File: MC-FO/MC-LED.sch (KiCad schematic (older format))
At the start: 14 parts, among them U21 TPS3703A5330DSER, U22 74ACT08SCX, U23 TPS3703A5500DSER, U24 TPS3703A5330DSER

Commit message: floating pins fix, signal name updates
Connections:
- wire segments 70 -> 76
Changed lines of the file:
@@
 	2550 2150 2500 2150
 Wire Wire Line
-	2500 2150 2500 2750
+	2500 2150 2500 2550
 Wire Wire Line
 	2500 2750 2400 2750
@@
 	4800 2150 4750 2150
 Wire Wire Line
-	4750 2150 4750 2750
+	4750 2150 4750 2550
 Wire Wire Line
 	4750 2750 4650 2750
@@
 	9350 2150 9250 2150
 Wire Wire Line
-	9250 2150 9250 2750
+	9250 2150 9250 2550
 Wire Wire Line
 	9250 2750 9000 2750
@@
 U 1 1 61797676
 P 3750 5000
+AR Path="/61797676" Ref="D1"  Part="1"
+AR Path="/6175812E/61797676" Ref="D1"  Part="1"
 F 0 "D1" V 3789 4782 50  0000 R CNN
 F 1 "550-2207-004F" V 3698 4782 50  0000 R CNN
@@
 U 1 1 6179851C
 P 9300 4000
+AR Path="/6179851C" Ref="D2"  Part="1"
+AR Path="/6175812E/6179851C" Ref="D2"  Part="1"
 F 0 "D2" V 9339 3782 50  0000 R CNN
 F 1 "550-2207-004F" V 9248 3782 50  0000 R CNN
@@
 	0    -1   -1   0
 $EndComp
+Wire Wire Line
+	9250 2550 9000 2550
+Connection ~ 9250 2550
+Wire Wire Line
+	9250 2550 9250 2750
+Wire Wire Line
+	4750 2550 4650 2550
+Connection ~ 4750 2550
+Wire Wire Line
+	4750 2550 4750 2750
+Wire Wire Line
+	2400 2550 2500 2550
+Connection ~ 2500 2550
+Wire Wire Line
+	2500 2550 2500 2750
 $EndSCHEMATC

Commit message: Fixed floating pins, added notes
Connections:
- wire segments 76 -> 100
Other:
- note added: "Voltage Drop Considerations?\n"
- moved on the sheet: R20
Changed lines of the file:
@@
 Comment4 ""
 $EndDescr
-Text Notes 2750 6050 0    50   ~ 10
+Text Notes 2750 6350 0    50   ~ 10
 Power Indicator LED CKT
 $Comp
 L Device:R_US R20
 U 1 1 61706570
-P 3850 4350
-F 0 "R20" H 3700 4250 50  0000 C CNN
-F 1 "500 Ohm" H 3600 4350 50  0000 C CNN
-F 2 "Resistor_SMD:R_0603_1608Metric" V 3890 4340 50  0001 C CNN
-F 3 "~" H 3850 4350 50  0001 C CNN
-	1    3850 4350
+P 3850 4650
+F 0 "R20" H 3700 4550 50  0000 C CNN
+F 1 "500 Ohm" H 3600 4650 50  0000 C CNN
+F 2 "Resistor_SMD:R_0603_1608Metric" V 3890 4640 50  0001 C CNN
+F 3 "~" H 3850 4650 50  0001 C CNN
+	1    3850 4650
 	-1   0    0    1
 $EndComp
 Wire Wire Line
-	3850 5150 3850 5450
+	3850 5450 3850 5750
 Text Notes 8350 4950 0    50   ~ 10
 Module Status LED CKT
@@
 	9400 4150 9400 4450
 Wire Wire Line
-	3850 5450 4050 5450
+	3850 5750 4050 5750
 Text HLabel 7950 2150 0    50   Input ~ 0
 StatusLED
-Text HLabel 4050 5450 2    50   Input ~ 0
+Text HLabel 4050 5750 2    50   Input ~ 0
 GND1
 Text HLabel 9650 4450 2    50   Input ~ 0
@@
 	4900 2950 4900 3900
 Wire Wire Line
-	3400 4000 3850 4000
-Wire Wire Line
-	3850 4000 3850 4200
-Wire Wire Line
-	3850 4500 3850 4850
+	3850 4300 3850 4500
+Wire Wire Line
+	3850 4800 3850 5150
 Text HLabel 2950 2150 2    50   Input ~ 0
 3V3
@@
 L Existing_IC_Models:550-0207-010-1163401 D1
 U 1 1 61797676
-P 3750 5000
+P 3750 5300
 AR Path="/61797676" Ref="D1"  Part="1"
 AR Path="/6175812E/61797676" Ref="D1"  Part="1"
-F 0 "D1" V 3789 4782 50  0000 R CNN
-F 1 "550-2207-004F" V 3698 4782 50  0000 R CNN
-F 2 "Footprints_MC-FO:550-2207-004F" H 3750 5100 50  0001 C CNN
-F 3 "" H 3750 5100 50  0001 C CNN
-	1    3750 5000
+F 0 "D1" V 3789 5082 50  0000 R CNN
+F 1 "550-2207-004F" V 3698 5082 50  0000 R CNN
+F 2 "Footprints_MC-FO:550-2207-004F" H 3750 5400 50  0001 C CNN
+F 3 "" H 3750 5400 50  0001 C CNN
+	1    3750 5300
 	0    -1   -1   0
 $EndComp
@@
 Wire Wire Line
 	2500 2550 2500 2750
+Text Notes 8200 1700 0    50   ~ 0
+Voltage Drop Considerations?\n
+Wire Wire Line
+	2600 3900 2400 3900
+Wire Wire Line
+	2400 3900 2400 4200
+Wire Wire Line
+	2400 4200 2600 4200
+Wire Wire Line
+	2400 4200 2400 4550
+Wire Wire Line
+	2400 4550 3500 4550
+Wire Wire Line
+	3500 4550 3500 4300
+Wire Wire Line
+	3500 4300 3400 4300
+Connection ~ 2400 4200
+Wire Wire Line
+	3500 4300 3850 4300
+Connection ~ 3500 4300
+Wire Wire Line
+	3650 4000 3650 4100
+Wire Wire Line
+	3400 4000 3650 4000
+Wire Wire Line
+	3400 4100 3650 4100
+Wire Wire Line
+	3650 4100 3650 4700
+Wire Wire Line
+	3650 4700 2300 4700
+Wire Wire Line
+	2300 4700 2300 4100
+Wire Wire Line
+	2300 3800 2600 3800
+Connection ~ 3650 4100
+Wire Wire Line
+	2300 4100 2600 4100
+Connection ~ 2300 4100
+Wire Wire Line
+	2300 4100 2300 3800
+Text HLabel 2050 3450 0    50   Input ~ 0
+5V
+Text HLabel 4050 3700 2    50   Input ~ 0
+5V
+Wire Wire Line
+	4050 3700 3800 3700
+Wire Wire Line
+	3800 3700 3800 4200
+Wire Wire Line
+	3800 4200 3400 4200
+Wire Wire Line
+	2050 3450 2150 3450
+Wire Wire Line
+	2150 3450 2150 3700
+Wire Wire Line
+	2150 3700 2600 3700
+Wire Wire Line
+	2150 3700 2150 4000
+Wire Wire Line
+	2150 4000 2600 4000
+Connection ~ 2150 3700
 $EndSCHEMATC

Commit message: unpopulated cap after voltage regulators
and changed reference designator numbering scheme
and moved the or gate that sends 3.3 V to comparator in detector ckt
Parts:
- D181: renamed from D1; symbol Existing_IC_Models:550-0207-010-1163401 -> Existing_IC_Models:550-2207-004F
- D182: renamed from D2; symbol Existing_IC_Models:550-0207-010-1163401 -> Existing_IC_Models:550-2207-004F
- renumbered C35 to C181, C36 to C182, C37 to C183, R19 to R181, R20 to R182, R21 to R183, R22 to R184, R23 to R185, U21 to U181, U22 to U182, U23 to U183, U24 to U184
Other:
- note added: "add comparatorson both and logically AND together for LED on power status\n\n\n (windowed comparators or voltage supervisors)"
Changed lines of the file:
@@
 Power Indicator LED CKT
 $Comp
-L Device:R_US R20
+L Device:R_US R182
 U 1 1 61706570
 P 3850 4650
-F 0 "R20" H 3700 4550 50  0000 C CNN
+F 0 "R182" H 3700 4550 50  0000 C CNN
 F 1 "500 Ohm" H 3600 4650 50  0000 C CNN
 F 2 "Resistor_SMD:R_0603_1608Metric" V 3890 4640 50  0001 C CNN
@@
 Module Status LED CKT
 $Comp
-L Device:R_US R22
+L Device:R_US R184
 U 1 1 61713526
 P 9400 3450
-F 0 "R22" H 9250 3350 50  0000 C CNN
+F 0 "R184" H 9250 3350 50  0000 C CNN
 F 1 "500 Ohm" H 9150 3450 50  0000 C CNN
 F 2 "Resistor_SMD:R_0603_1608Metric" V 9440 3440 50  0001 C CNN
@@
 5V
 $Comp
-L Existing_IC_Models:74ACT08SCX U22
+L Existing_IC_Models:74ACT08SCX U182
 U 1 1 6176E3CF
 P 3000 3550
-F 0 "U22" H 3000 3665 50  0000 C CNN
+F 0 "U182" H 3000 3665 50  0000 C CNN
 F 1 "74ACT08SCX" H 3000 3574 50  0000 C CNN
 F 2 "Package_SO:SOIC-14_3.9x8.7mm_P1.27mm" H 3000 3550 50  0001 C CNN
@@
 $EndComp
 $Comp
-L Existing_IC_Models:TPS3703A5500DSER U23
+L Existing_IC_Models:TPS3703A5500DSER U183
 U 1 1 6177F576
 P 4250 2250
-F 0 "U23" H 4250 2215 50  0000 C CNN
+F 0 "U183" H 4250 2215 50  0000 C CNN
 F 1 "TPS3703A5500DSER" H 4250 2124 50  0000 C CNN
 F 2 "Package_SON:WSON-6_1.5x1.5mm_P0.5mm" H 4250 2250 50  0001 C CNN
@@
 $EndComp
 $Comp
-L Existing_IC_Models:TPS3703A5330DSER U21
+L Existing_IC_Models:TPS3703A5330DSER U181
 U 1 1 61781150
 P 2000 2250
-F 0 "U21" H 2000 2215 50  0000 C CNN
+F 0 "U181" H 2000 2215 50  0000 C CNN
 F 1 "TPS3703A5330DSER" H 2000 2124 50  0000 C CNN
 F 2 "Package_SON:WSON-6_1.5x1.5mm_P0.5mm" H 2000 2250 50  0001 C CNN
@@
 3V3
 $Comp
-L Device:R_Small_US R19
+L Device:R_Small_US R181
 U 1 1 617C2D42
 P 2900 2700
-F 0 "R19" H 2968 2746 50  0000 L CNN
+F 0 "R181" H 2968 2746 50  0000 L CNN
 F 1 "10 K" H 2968 2655 50  0000 L CNN
 F 2 "Resistor_SMD:R_0603_1608Metric" H 2900 2700 50  0001 C CNN
@@
 $EndComp
 $Comp
-L Device:R_Small_US R21
+L Device:R_Small_US R183
 U 1 1 617C3F20
 P 5200 2550
-F 0 "R21" H 5268 2596 50  0000 L CNN
+F 0 "R183" H 5268 2596 50  0000 L CNN
 F 1 "10 K" H 5268 2505 50  0000 L CNN
 F 2 "Resistor_SMD:R_0603_1608Metric" H 5200 2550 50  0001 C CNN
@@
 Connection ~ 4900 2950
 $Comp
-L Device:C_Small C35
+L Device:C_Small C181
 U 1 1 617CFF8B
 P 1350 3100
-F 0 "C35" H 1442 3146 50  0000 L CNN
+F 0 "C181" H 1442 3146 50  0000 L CNN
 F 1 "1 uF" H 1442 3055 50  0000 L CNN
 F 2 "Capacitor_SMD:C_0603_1608Metric" H 1350 3100 50  0001 C CNN
@@
 $EndComp
 $Comp
-L Device:C_Small C36
+L Device:C_Small C182
 U 1 1 617D05D8
 P 3800 3300
-F 0 "C36" H 3892 3346 50  0000 L CNN
+F 0 "C182" H 3892 3346 50  0000 L CNN
 F 1 "1 uF" H 3892 3255 50  0000 L CNN
 F 2 "Capacitor_SMD:C_0603_1608Metric" H 3800 3300 50  0001 C CNN
@@
 	3800 3550 4050 3550
 $Comp
-L Existing_IC_Models:TPS3703A5330DSER U24
+L Existing_IC_Models:TPS3703A5330DSER U184
 U 1 1 617FD968
 P 8600 2250
-F 0 "U24" H 8600 2215 50  0000 C CNN
+F 0 "U184" H 8600 2215 50  0000 C CNN
 F 1 "TPS3703A5330DSER" H 8600 2124 50  0000 C CNN
 F 2 "Package_SON:WSON-6_1.5x1.5mm_P0.5mm" H 8600 2250 50  0001 C CNN
@@
 3V3
 $Comp
-L Device:C_Small C37
+L Device:C_Small C183
 U 1 1 6180E36A
 P 8150 3250
-F 0 "C37" H 8242 3296 50  0000 L CNN
+F 0 "C183" H 8242 3296 50  0000 L CNN
 F 1 "1 uF" H 8242 3205 50  0000 L CNN
 F 2 "Capacitor_SMD:C_0603_1608Metric" H 8150 3250 50  0001 C CNN
@@
 3V3
 $Comp
-L Device:R_Small_US R23
+L Device:R_Small_US R185
 U 1 1 61820038
 P 9750 2500
-F 0 "R23" H 9818 2546 50  0000 L CNN
+F 0 "R185" H 9818 2546 50  0000 L CNN
 F 1 "10 K" H 9818 2455 50  0000 L CNN
 F 2 "Resistor_SMD:R_0603_1608Metric" H 9750 2500 50  0001 C CNN
@@
 	9650 4450 9400 4450
 $Comp
-L Existing_IC_Models:550-0207-010-1163401 D1
+L Existing_IC_Models:550-2207-004F D?
 U 1 1 61797676
 P 3750 5300
-AR Path="/61797676" Ref="D1"  Part="1"
-AR Path="/6175812E/61797676" Ref="D1"  Part="1"
-F 0 "D1" V 3789 5082 50  0000 R CNN
+AR Path="/61797676" Ref="D?"  Part="1"
+AR Path="/6175812E/61797676" Ref="D181"  Part="1"
+F 0 "D181" V 3789 5082 50  0000 R CNN
 F 1 "550-2207-004F" V 3698 5082 50  0000 R CNN
 F 2 "Footprints_MC-FO:550-2207-004F" H 3750 5400 50  0001 C CNN
@@
 $EndComp
 $Comp
-L Existing_IC_Models:550-0207-010-1163401 D2
+L Existing_IC_Models:550-2207-004F D?
 U 1 1 6179851C
 P 9300 4000
-AR Path="/6179851C" Ref="D2"  Part="1"
-AR Path="/6175812E/6179851C" Ref="D2"  Part="1"
-F 0 "D2" V 9339 3782 50  0000 R CNN
+AR Path="/6179851C" Ref="D?"  Part="1"
+AR Path="/6175812E/6179851C" Ref="D182"  Part="1"
+F 0 "D182" V 9339 3782 50  0000 R CNN
 F 1 "550-2207-004F" V 9248 3782 50  0000 R CNN
 F 2 "Footprints_MC-FO:550-2207-004F" H 9300 4100 50  0001 C CNN
@@
 	2150 4000 2600 4000
 Connection ~ 2150 3700
+Text Notes 4050 7350 2    50   ~ 0
+add comparatorson both and logically AND together for LED on power status\n\n\n (windowed comparators or voltage supervisors)
 $EndSCHEMATC

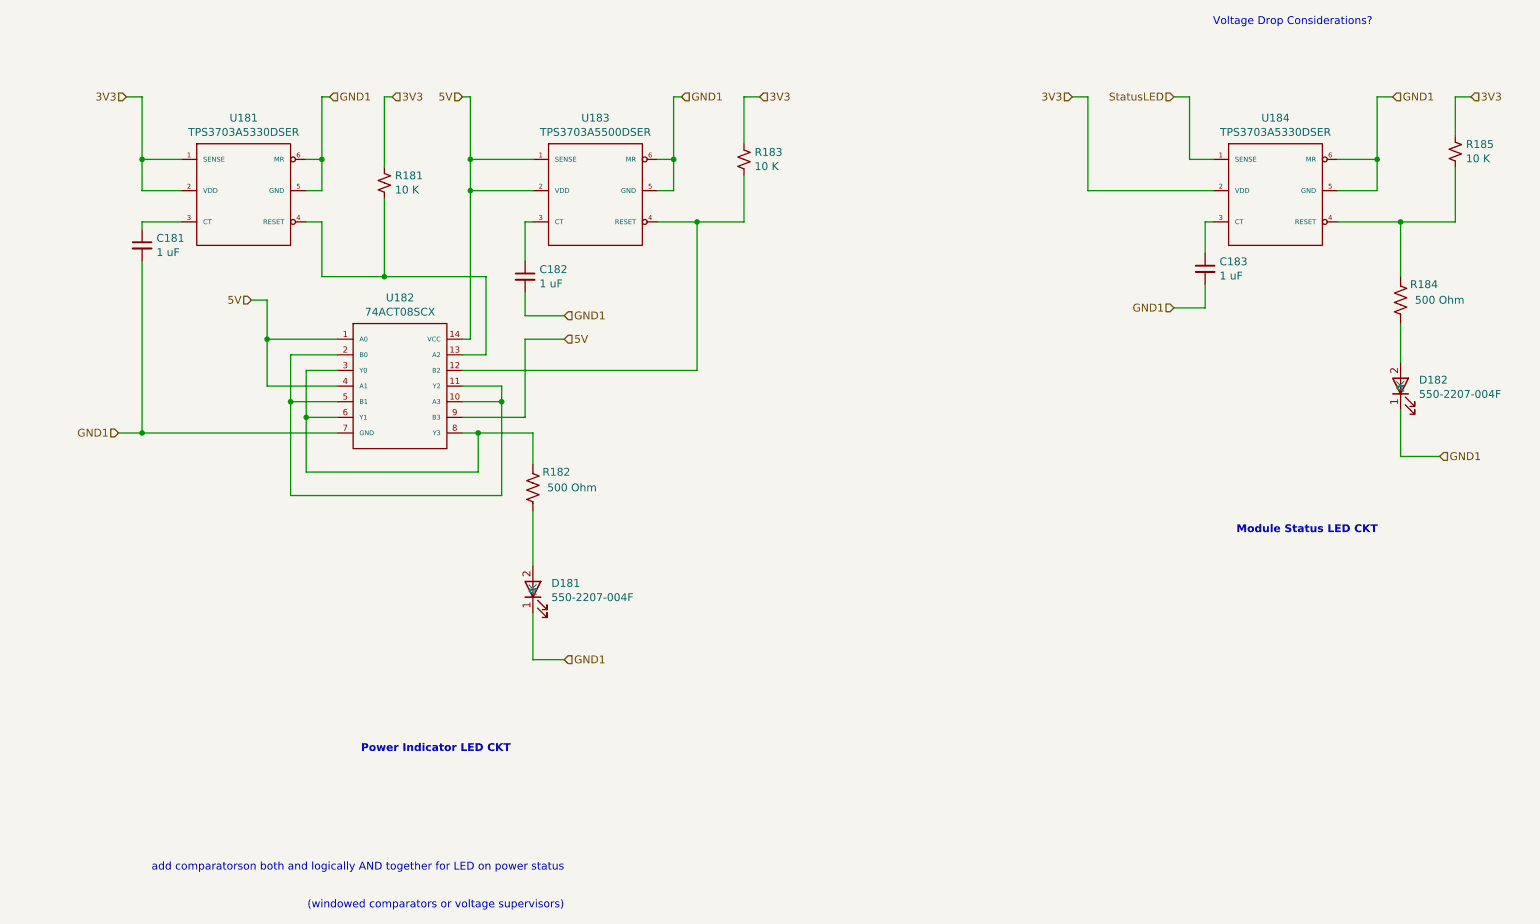
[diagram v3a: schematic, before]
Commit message: Fixed file hierarchy
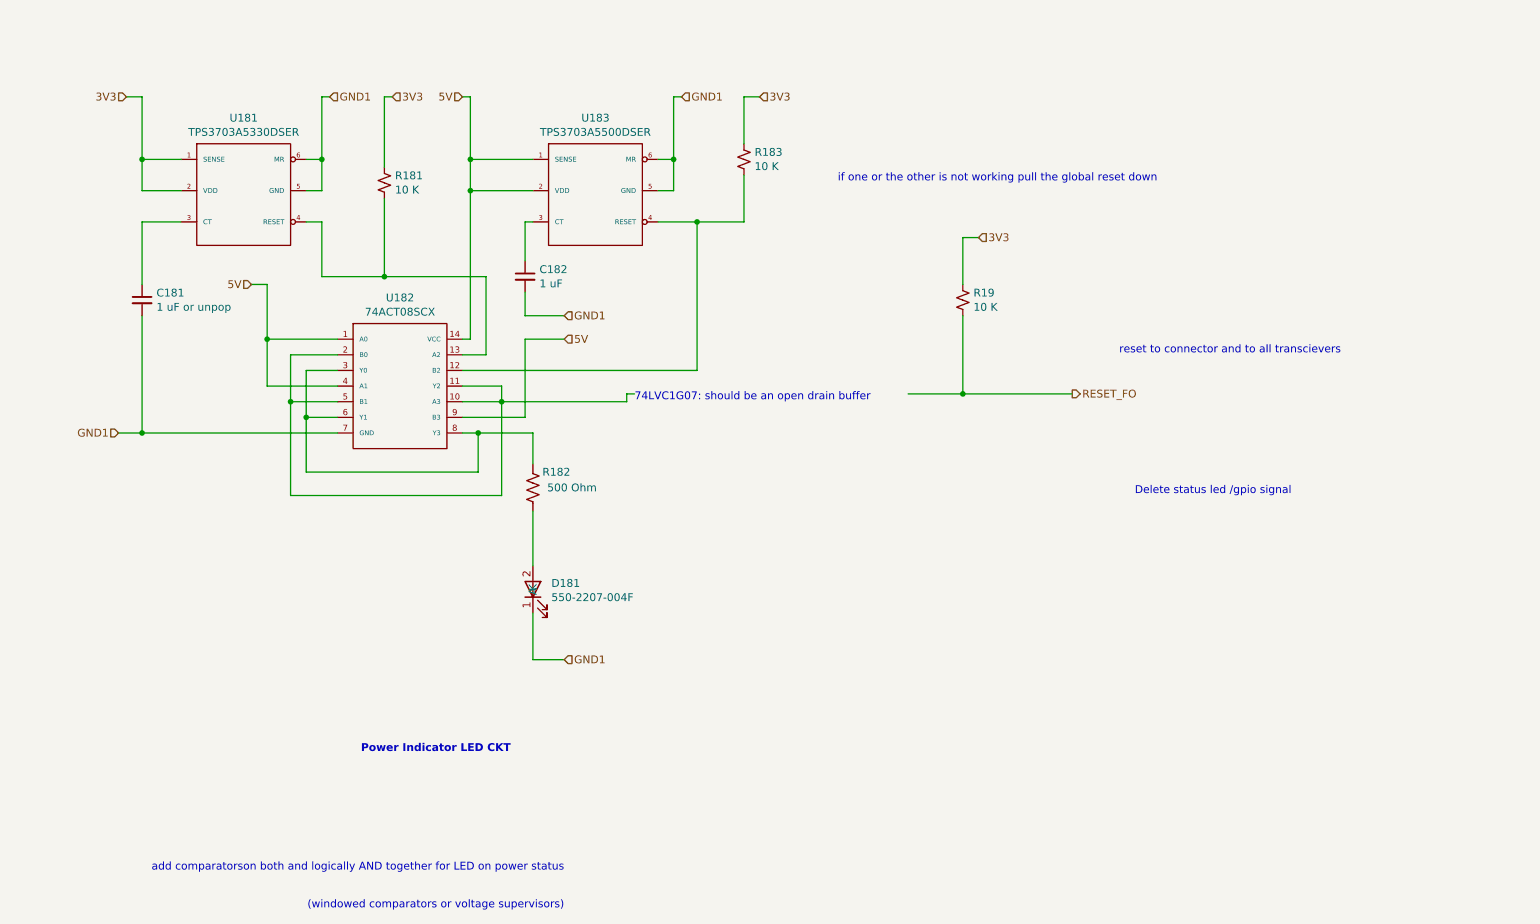
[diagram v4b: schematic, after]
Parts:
- removed C183: 1 uF, Capacitor_SMD:C_0603_1608Metric, symbol Device:C_Small
- removed D182: 550-2207-004F, Footprints_MC-FO:550-2207-004F, symbol Existing_IC_Models:550-2207-004F
- removed R184: 500 Ohm, Resistor_SMD:R_0603_1608Metric, symbol Device:R_US
- removed R185: 10 K, Resistor_SMD:R_0603_1608Metric, symbol Device:R_Small_US
- removed U184: TPS3703A5330DSER, Package_SON:WSON-6_1.5x1.5mm_P0.5mm, symbol Existing_IC_Models:TPS3703A5330DSER
- added R19: 10 K, Resistor_SMD:R_0603_1608Metric, symbol Device:R_Small_US
- C181: value 1 uF -> 1 uF or unpop
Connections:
- net 3V3: now also R19.1
- new net RESET_FO: R19.2
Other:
- note added: "74LVC1G07: should be an open drain buffer\n"
- note added: "Delete status led /gpio signal"
- note added: "if one or the other is not working pull the global reset down"
- note added: "reset to connector and to all transcievers"
- note removed: "Module Status LED CKT"
- note removed: "Voltage Drop Considerations?\n"
- moved on the sheet: C181
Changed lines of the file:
@@
 $Descr A4 11693 8268
 encoding utf-8
-Sheet 11 11
+Sheet 9 11
 Title ""
 Date ""
@@
 Wire Wire Line
 	3850 5450 3850 5750
-Text Notes 8350 4950 0    50   ~ 10
-Module Status LED CKT
-$Comp
-L Device:R_US R184
-U 1 1 61713526
-P 9400 3450
-F 0 "R184" H 9250 3350 50  0000 C CNN
-F 1 "500 Ohm" H 9150 3450 50  0000 C CNN
-F 2 "Resistor_SMD:R_0603_1608Metric" V 9440 3440 50  0001 C CNN
-F 3 "~" H 9400 3450 50  0001 C CNN
-	1    9400 3450
-	-1   0    0    1
-$EndComp
-Wire Wire Line
-	9400 4150 9400 4450
 Wire Wire Line
 	3850 5750 4050 5750
-Text HLabel 7950 2150 0    50   Input ~ 0
-StatusLED
 Text HLabel 4050 5750 2    50   Input ~ 0
-GND1
-Text HLabel 9650 4450 2    50   Input ~ 0
 GND1
 Text HLabel 3400 2150 0    50   Input ~ 0
@@
 L Device:C_Small C181
 U 1 1 617CFF8B
-P 1350 3100
-F 0 "C181" H 1442 3146 50  0000 L CNN
-F 1 "1 uF" H 1442 3055 50  0000 L CNN
-F 2 "Capacitor_SMD:C_0603_1608Metric" H 1350 3100 50  0001 C CNN
-F 3 "~" H 1350 3100 50  0001 C CNN
-	1    1350 3100
+P 1350 3450
+F 0 "C181" H 1442 3496 50  0000 L CNN
+F 1 "1 uF or unpop" H 1442 3405 50  0000 L CNN
+F 2 "Capacitor_SMD:C_0603_1608Metric" H 1350 3450 50  0001 C CNN
+F 3 "~" H 1350 3450 50  0001 C CNN
+	1    1350 3450
 	1    0    0    -1
 $EndComp
@@
 	1600 2950 1350 2950
 Wire Wire Line
-	1350 2950 1350 3000
+	1350 2950 1350 3350
 Text HLabel 1200 4300 0    50   Input ~ 0
 GND1
@@
 	2600 4300 1350 4300
 Wire Wire Line
-	1350 4300 1350 3200
+	1350 4300 1350 3550
 Wire Wire Line
 	1350 4300 1200 4300
@@
 Wire Wire Line
 	3800 3550 4050 3550
-$Comp
-L Existing_IC_Models:TPS3703A5330DSER U184
-U 1 1 617FD968
-P 8600 2250
-F 0 "U184" H 8600 2215 50  0000 C CNN
-F 1 "TPS3703A5330DSER" H 8600 2124 50  0000 C CNN
-F 2 "Package_SON:WSON-6_1.5x1.5mm_P0.5mm" H 8600 2250 50  0001 C CNN
-F 3 "" H 8600 2250 50  0001 C CNN
-	1    8600 2250
-	1    0    0    -1
-$EndComp
-Text HLabel 7300 2150 0    50   Input ~ 0
-3V3
-$Comp
-L Device:C_Small C183
-U 1 1 6180E36A
-P 8150 3250
-F 0 "C183" H 8242 3296 50  0000 L CNN
-F 1 "1 uF" H 8242 3205 50  0000 L CNN
-F 2 "Capacitor_SMD:C_0603_1608Metric" H 8150 3250 50  0001 C CNN
-F 3 "~" H 8150 3250 50  0001 C CNN
-	1    8150 3250
-	1    0    0    -1
-$EndComp
-Wire Wire Line
-	8200 2950 8150 2950
-Wire Wire Line
-	8150 2950 8150 3150
-Wire Wire Line
-	8150 3350 8150 3500
-Text HLabel 7950 3500 0    50   Input ~ 0
-GND1
-Wire Wire Line
-	8150 3500 7950 3500
-Text HLabel 9350 2150 2    50   Input ~ 0
-GND1
-Text HLabel 9850 2150 2    50   Input ~ 0
-3V3
-$Comp
-L Device:R_Small_US R185
-U 1 1 61820038
-P 9750 2500
-F 0 "R185" H 9818 2546 50  0000 L CNN
-F 1 "10 K" H 9818 2455 50  0000 L CNN
-F 2 "Resistor_SMD:R_0603_1608Metric" H 9750 2500 50  0001 C CNN
-F 3 "~" H 9750 2500 50  0001 C CNN
-	1    9750 2500
-	1    0    0    -1
-$EndComp
-Wire Wire Line
-	9850 2150 9750 2150
-Wire Wire Line
-	9750 2150 9750 2400
-Wire Wire Line
-	9750 2600 9750 2950
-Wire Wire Line
-	9750 2950 9400 2950
-Wire Wire Line
-	9400 2950 9400 3300
-Wire Wire Line
-	9400 2950 9000 2950
-Connection ~ 9400 2950
-Wire Wire Line
-	9350 2150 9250 2150
-Wire Wire Line
-	9250 2150 9250 2550
-Wire Wire Line
-	9250 2750 9000 2750
-Wire Wire Line
-	7950 2150 8050 2150
-Wire Wire Line
-	8050 2150 8050 2550
-Wire Wire Line
-	8050 2550 8200 2550
-Wire Wire Line
-	7300 2150 7400 2150
-Wire Wire Line
-	7400 2150 7400 2750
-Wire Wire Line
-	7400 2750 8200 2750
-Wire Wire Line
-	9400 3600 9400 3850
-Wire Wire Line
-	9650 4450 9400 4450
 $Comp
 L Existing_IC_Models:550-2207-004F D?
@@
 	0    -1   -1   0
 $EndComp
-$Comp
-L Existing_IC_Models:550-2207-004F D?
-U 1 1 6179851C
-P 9300 4000
-AR Path="/6179851C" Ref="D?"  Part="1"
-AR Path="/6175812E/6179851C" Ref="D182"  Part="1"
-F 0 "D182" V 9339 3782 50  0000 R CNN
-F 1 "550-2207-004F" V 9248 3782 50  0000 R CNN
-F 2 "Footprints_MC-FO:550-2207-004F" H 9300 4100 50  0001 C CNN
-F 3 "" H 9300 4100 50  0001 C CNN
-	1    9300 4000
-	0    -1   -1   0
-$EndComp
-Wire Wire Line
-	9250 2550 9000 2550
-Connection ~ 9250 2550
-Wire Wire Line
-	9250 2550 9250 2750
 Wire Wire Line
 	4750 2550 4650 2550
@@
 Wire Wire Line
 	2500 2550 2500 2750
-Text Notes 8200 1700 0    50   ~ 0
-Voltage Drop Considerations?\n
 Wire Wire Line
 	2600 3900 2400 3900
@@
 Wire Wire Line
 	2300 4100 2300 3800
-Text HLabel 2050 3450 0    50   Input ~ 0
+Text HLabel 2050 3350 0    50   Input ~ 0
 5V
 Text HLabel 4050 3700 2    50   Input ~ 0
@@
 	3800 4200 3400 4200
 Wire Wire Line
-	2050 3450 2150 3450
-Wire Wire Line
-	2150 3450 2150 3700
+	2050 3350 2150 3350
+Wire Wire Line
+	2150 3350 2150 3700
 Wire Wire Line
 	2150 3700 2600 3700
@@
 Text Notes 4050 7350 2    50   ~ 0
 add comparatorson both and logically AND together for LED on power status\n\n\n (windowed comparators or voltage supervisors)
+Text Notes 7700 4700 0    50   ~ 0
+Delete status led /gpio signal
+Text Notes 5800 2700 0    50   ~ 0
+if one or the other is not working pull the global reset down
+Text Notes 4500 4100 0    50   ~ 0
+74LVC1G07: should be an open drain buffer\n
+Wire Wire Line
+	3650 4100 4450 4100
+Wire Wire Line
+	4450 4100 4450 4050
+Wire Wire Line
+	4450 4050 4500 4050
+Wire Wire Line
+	6250 4050 6600 4050
+Text Notes 7600 3800 0    50   ~ 0
+reset to connector and to all transcievers
+Connection ~ 6600 4050
+Wire Wire Line
+	6600 4050 7300 4050
+$Comp
+L Device:R_Small_US R19
+U 1 1 6182FD38
+P 6600 3450
+F 0 "R19" H 6668 3496 50  0000 L CNN
+F 1 "10 K" H 6668 3405 50  0000 L CNN
+F 2 "Resistor_SMD:R_0603_1608Metric" H 6600 3450 50  0001 C CNN
+F 3 "~" H 6600 3450 50  0001 C CNN
+	1    6600 3450
+	1    0    0    -1
+$EndComp
+Text HLabel 6700 3050 2    50   Input ~ 0
+3V3
+Wire Wire Line
+	6700 3050 6600 3050
+Wire Wire Line
+	6600 3050 6600 3350
+Wire Wire Line
+	6600 3550 6600 4050
+Text HLabel 7300 4050 2    50   Output ~ 0
+RESET_FO
 $EndSCHEMATC
